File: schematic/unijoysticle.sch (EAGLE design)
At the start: 8 parts, among them CN1 DC JACK, IC1 4066N, IC2 4066N, IC3 4066N, J1 DB9, J2 DB9

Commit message: fix: yet another pcb version. smaller, better design
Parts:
- MOD1: value NodeMCU Amica v1.0 -> ESP12E_DEVKIT; OC_NEWARK unknown -> (none)
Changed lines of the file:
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@@
 </classes>
 <parts>
-<part name="MOD1" library="ESP12E_DEVKIT" deviceset="ESP12E_DEVKIT" device="" value="NodeMCU Amica v1.0">
-<attribute name="MF" value=""/>
-<attribute name="MPN" value=""/>
-<attribute name="OC_NEWARK" value="unknown"/>
-</part>
 <part name="IC1" library="40xx" deviceset="4066" device="N">
 <attribute name="MF" value="TEXAS INSTRUMENTS"/>
@@
 <attribute name="OC_NEWARK" value="16T0655"/>
 </part>
+<part name="MOD1" library="ESP12E_DEVKIT" deviceset="ESP12E_DEVKIT" device=""/>
 </parts>
 <sheets>
@@
 </plain>
 <instances>
-<instance part="MOD1" gate="G$1" x="116.84" y="25.4" rot="R90">
-<attribute name="OC_NEWARK" x="116.84" y="25.4" size="1.778" layer="96" display="off"/>
-<attribute name="MF" x="116.84" y="25.4" size="1.778" layer="96" display="off"/>
-<attribute name="MPN" x="116.84" y="25.4" size="1.778" layer="96" display="off"/>
-</instance>
 <instance part="IC1" gate="A" x="68.58" y="139.7">
 <attribute name="OC_NEWARK" x="68.58" y="139.7" size="1.778" layer="96" display="off"/>
@@
 <attribute name="MPN" x="154.94" y="170.18" size="1.778" layer="96" display="off"/>
 </instance>
+<instance part="MOD1" gate="G$1" x="116.84" y="25.4" rot="R90"/>
 </instances>
 <busses>
@@
 <net name="N$1" class="0">
 <segment>
-<pinref part="MOD1" gate="G$1" pin="D0"/>
 <wire x1="99.06" y1="43.18" x2="99.06" y2="48.26" width="0.1524" layer="91"/>
 <wire x1="99.06" y1="48.26" x2="22.86" y2="48.26" width="0.1524" layer="91"/>
@@
 <pinref part="IC1" gate="A" pin="C"/>
 <wire x1="22.86" y1="137.16" x2="55.88" y2="137.16" width="0.1524" layer="91"/>
+<pinref part="MOD1" gate="G$1" pin="D0"/>
 </segment>
 </net>
 <net name="N$2" class="0">
 <segment>
-<pinref part="MOD1" gate="G$1" pin="D1"/>
 <wire x1="101.6" y1="43.18" x2="101.6" y2="50.8" width="0.1524" layer="91"/>
 <wire x1="101.6" y1="50.8" x2="25.4" y2="50.8" width="0.1524" layer="91"/>
@@
 <pinref part="IC1" gate="B" pin="C"/>
 <wire x1="25.4" y1="119.38" x2="55.88" y2="119.38" width="0.1524" layer="91"/>
+<pinref part="MOD1" gate="G$1" pin="D1"/>
 </segment>
 </net>
 <net name="N$3" class="0">
 <segment>
-<pinref part="MOD1" gate="G$1" pin="D2"/>
 <wire x1="104.14" y1="43.18" x2="104.14" y2="53.34" width="0.1524" layer="91"/>
 <wire x1="104.14" y1="53.34" x2="27.94" y2="53.34" width="0.1524" layer="91"/>
@@
 <pinref part="IC1" gate="C" pin="C"/>
 <wire x1="27.94" y1="101.6" x2="55.88" y2="101.6" width="0.1524" layer="91"/>
+<pinref part="MOD1" gate="G$1" pin="D2"/>
 </segment>
 </net>
 <net name="N$4" class="0">
 <segment>
-<pinref part="MOD1" gate="G$1" pin="D3"/>
 <wire x1="106.68" y1="43.18" x2="106.68" y2="55.88" width="0.1524" layer="91"/>
 <wire x1="106.68" y1="55.88" x2="30.48" y2="55.88" width="0.1524" layer="91"/>
@@
 <pinref part="IC1" gate="D" pin="C"/>
 <wire x1="30.48" y1="83.82" x2="55.88" y2="83.82" width="0.1524" layer="91"/>
+<pinref part="MOD1" gate="G$1" pin="D3"/>
 </segment>
 </net>
 <net name="N$5" class="0">
 <segment>
-<pinref part="MOD1" gate="G$1" pin="D5"/>
 <wire x1="116.84" y1="43.18" x2="116.84" y2="137.16" width="0.1524" layer="91"/>
 <pinref part="IC3" gate="A" pin="C"/>
 <wire x1="116.84" y1="137.16" x2="142.24" y2="137.16" width="0.1524" layer="91"/>
+<pinref part="MOD1" gate="G$1" pin="D5"/>
 </segment>
 </net>
 <net name="N$6" class="0">
 <segment>
-<pinref part="MOD1" gate="G$1" pin="D6"/>
 <wire x1="119.38" y1="43.18" x2="119.38" y2="119.38" width="0.1524" layer="91"/>
 <pinref part="IC3" gate="B" pin="C"/>
 <wire x1="119.38" y1="119.38" x2="142.24" y2="119.38" width="0.1524" layer="91"/>
+<pinref part="MOD1" gate="G$1" pin="D6"/>
 </segment>
 </net>
 <net name="N$7" class="0">
 <segment>
-<pinref part="MOD1" gate="G$1" pin="D7"/>
 <wire x1="121.92" y1="43.18" x2="121.92" y2="101.6" width="0.1524" layer="91"/>
 <pinref part="IC3" gate="C" pin="C"/>
 <wire x1="121.92" y1="101.6" x2="142.24" y2="101.6" width="0.1524" layer="91"/>
+<pinref part="MOD1" gate="G$1" pin="D7"/>
 </segment>
 </net>
 <net name="N$8" class="0">
 <segment>
-<pinref part="MOD1" gate="G$1" pin="D8"/>
 <wire x1="124.46" y1="43.18" x2="124.46" y2="83.82" width="0.1524" layer="91"/>
 <pinref part="IC3" gate="D" pin="C"/>
 <wire x1="124.46" y1="83.82" x2="142.24" y2="83.82" width="0.1524" layer="91"/>
+<pinref part="MOD1" gate="G$1" pin="D8"/>
 </segment>
 </net>
@@
 </segment>
 <segment>
-<pinref part="MOD1" gate="G$1" pin="GND@3"/>
 <wire x1="132.08" y1="43.18" x2="132.08" y2="55.88" width="0.1524" layer="91"/>
 <wire x1="132.08" y1="55.88" x2="137.16" y2="55.88" width="0.1524" layer="91"/>
 <pinref part="GND3" gate="1" pin="GND"/>
 <wire x1="137.16" y1="55.88" x2="137.16" y2="53.34" width="0.1524" layer="91"/>
+<pinref part="MOD1" gate="G$1" pin="GND@3"/>
 </segment>
 </net>
@@
 </segment>
 <segment>
-<pinref part="MOD1" gate="G$1" pin="3V3@2"/>
 <pinref part="P+1" gate="VCC" pin="VCC"/>
 <wire x1="134.62" y1="43.18" x2="144.78" y2="43.18" width="0.1524" layer="91"/>
 <wire x1="144.78" y1="43.18" x2="144.78" y2="50.8" width="0.1524" layer="91"/>
+<pinref part="MOD1" gate="G$1" pin="3V3@2"/>
 </segment>
 </net>
 <net name="N$19" class="0">
 <segment>
-<pinref part="MOD1" gate="G$1" pin="D4"/>
 <wire x1="109.22" y1="43.18" x2="109.22" y2="58.42" width="0.1524" layer="91"/>
 <wire x1="109.22" y1="58.42" x2="50.8" y2="58.42" width="0.1524" layer="91"/>
@@
 <pinref part="IC2" gate="A" pin="C"/>
 <wire x1="50.8" y1="66.04" x2="55.88" y2="66.04" width="0.1524" layer="91"/>
+<pinref part="MOD1" gate="G$1" pin="D4"/>
 </segment>
 </net>
 <net name="N$20" class="0">
 <segment>
-<pinref part="MOD1" gate="G$1" pin="RX"/>
 <wire x1="127" y1="43.18" x2="127" y2="66.04" width="0.1524" layer="91"/>
 <pinref part="IC2" gate="B" pin="C"/>
 <wire x1="127" y1="66.04" x2="142.24" y2="66.04" width="0.1524" layer="91"/>
+<pinref part="MOD1" gate="G$1" pin="RX"/>
 </segment>
 </net>
@@
 <segment>
 <pinref part="SUPPLY2" gate="G$1" pin="5V"/>
+<wire x1="139.7" y1="7.62" x2="134.62" y2="7.62" width="0.1524" layer="91"/>
 <pinref part="MOD1" gate="G$1" pin="VIN"/>
-<wire x1="139.7" y1="7.62" x2="134.62" y2="7.62" width="0.1524" layer="91"/>
 </segment>
 </net>
@@
 </segment>
 <segment>
-<pinref part="MOD1" gate="G$1" pin="GND@1"/>
 <pinref part="GND2" gate="G$1" pin="3.3V"/>
 <wire x1="132.08" y1="0" x2="132.08" y2="7.62" width="0.1524" layer="91"/>
-</segment>
-</net>
+<pinref part="MOD1" gate="G$1" pin="GND@1"/>
+</segment>
+</net>

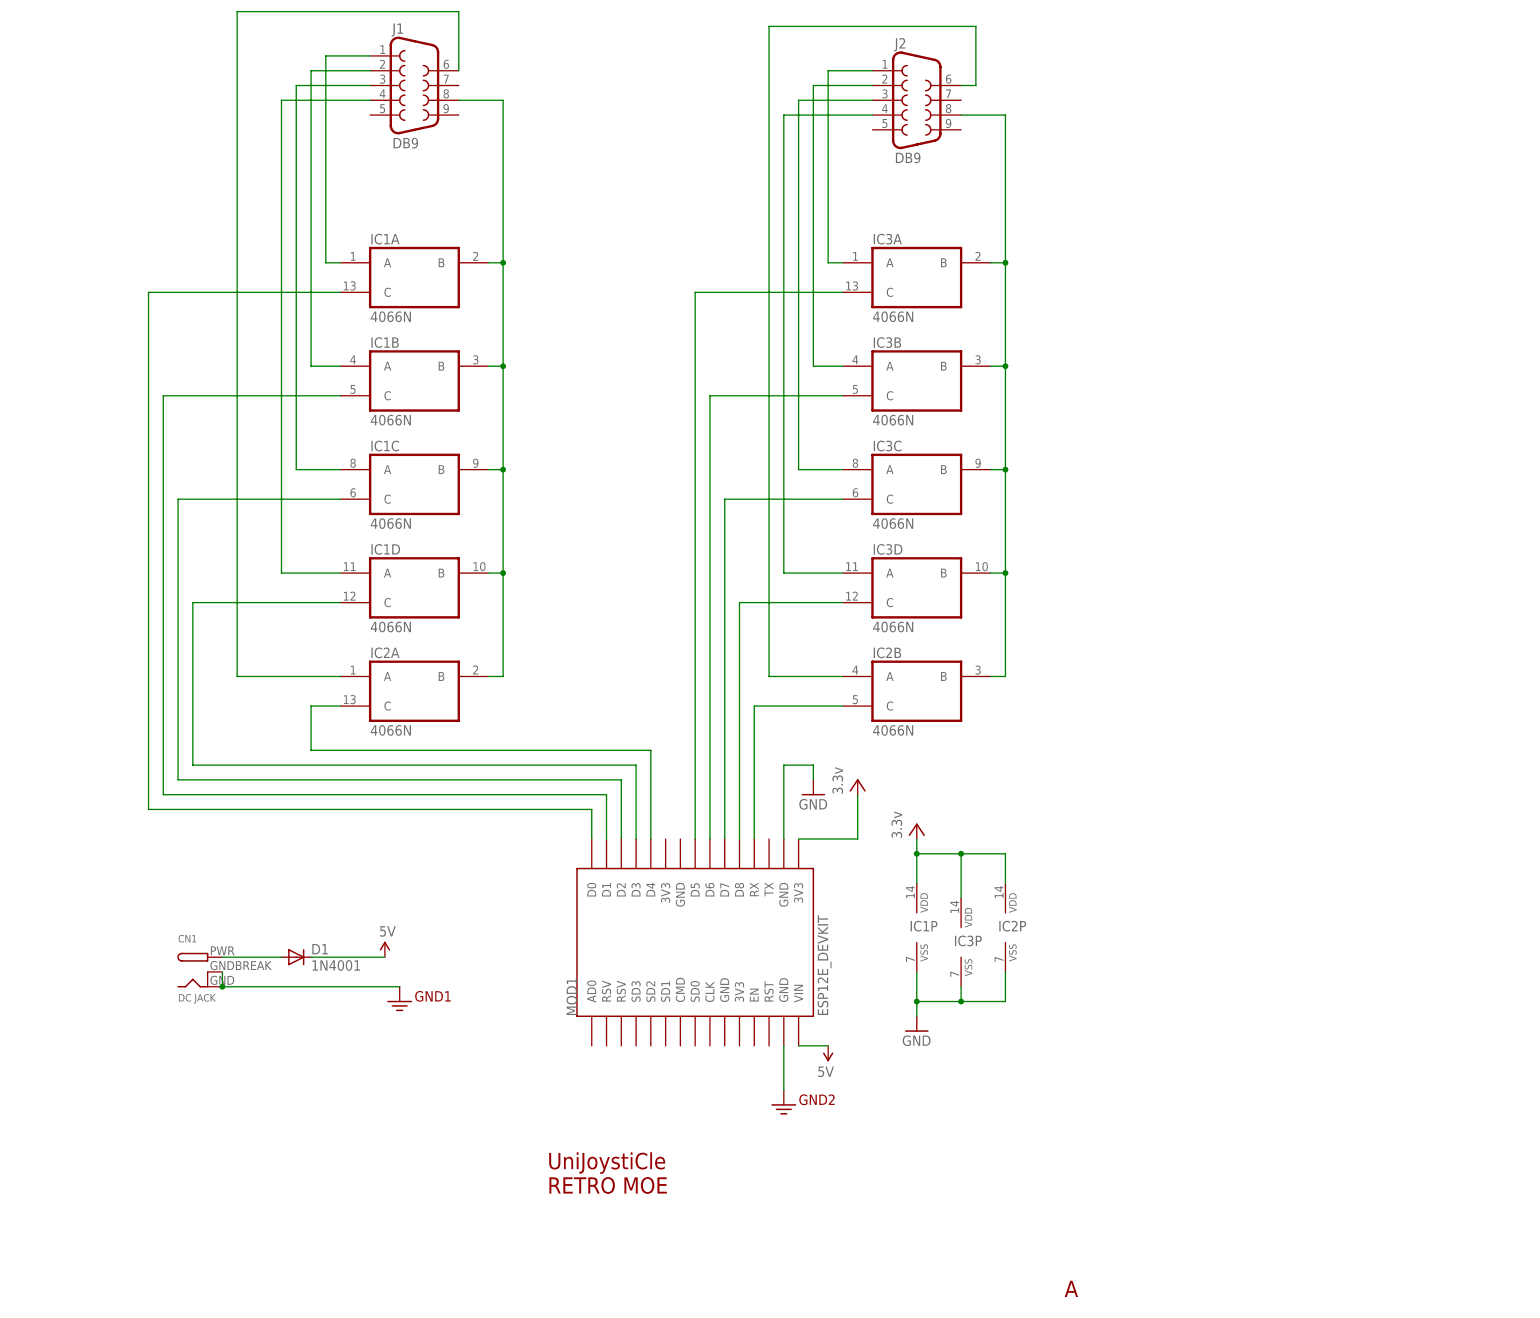
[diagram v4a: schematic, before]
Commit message: fix: adds .cam file to generate gerbert files
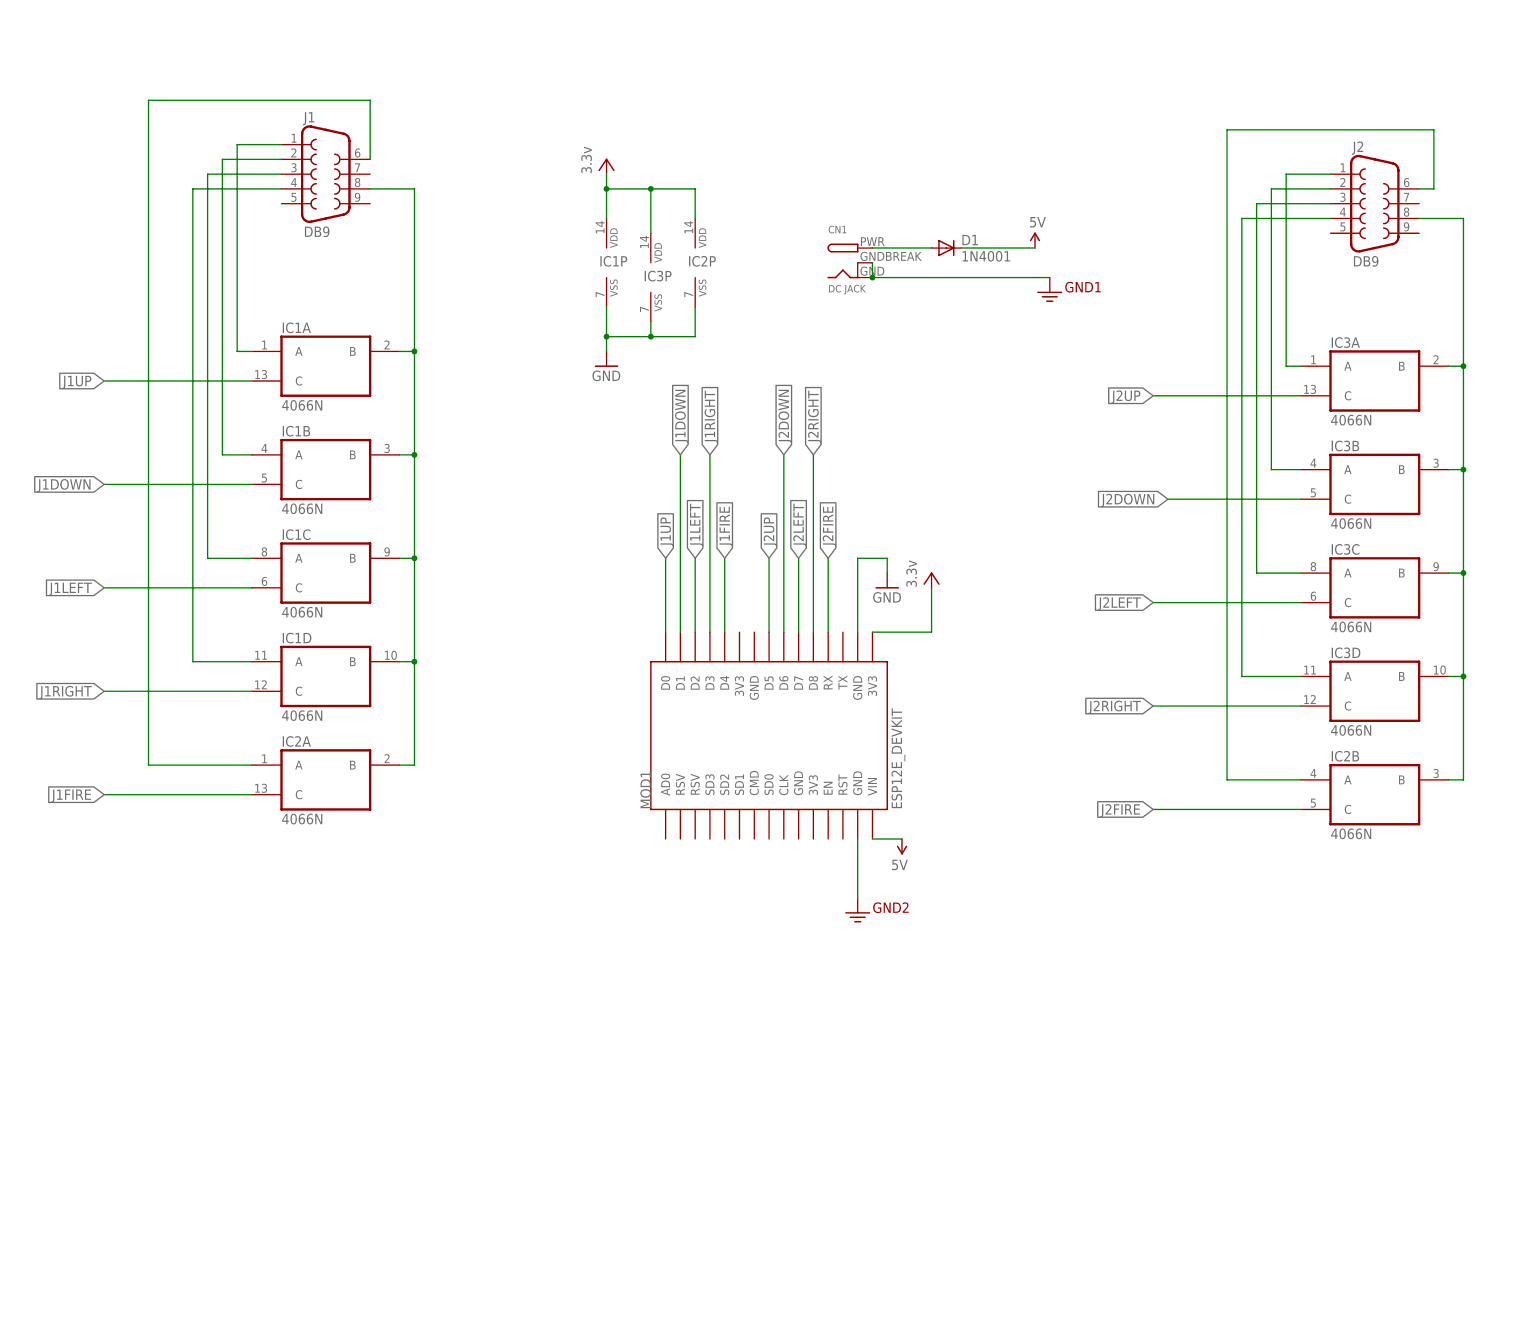
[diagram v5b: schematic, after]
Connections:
- net N$1 renamed J1UP
- net N$19 renamed J1FIRE
- net N$2 renamed J1DOWN
- net N$20 renamed J2FIRE
- net N$3 renamed J1LEFT
- net N$4 renamed J1RIGHT
- net N$5 renamed J2UP
- net N$6 renamed J2DOWN
- net N$7 renamed J2LEFT
- net N$8 renamed J2RIGHT
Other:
- note removed: "A"
- note removed: "UniJoystiCle RETRO MOE"
- moved on the sheet: CN1, D1, IC1A, IC1B, IC1C, IC1D, IC1P, IC2A, IC2B, IC2P, IC3A, IC3B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

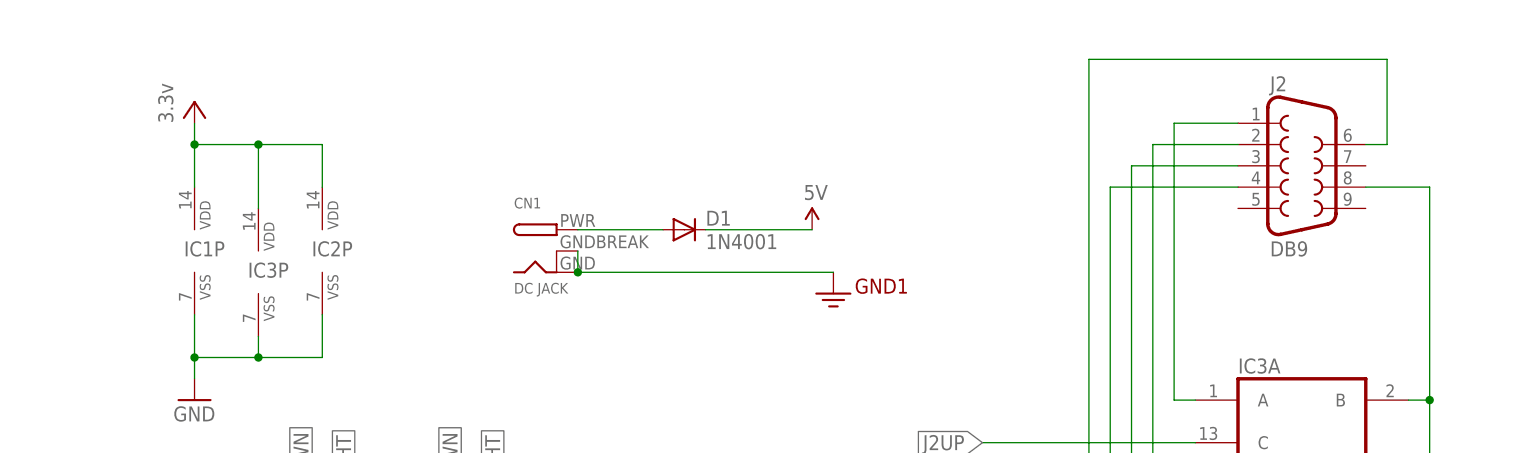
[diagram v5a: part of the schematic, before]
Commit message: fix: esp8622 schematic: ics with joy power. new dc jack barrel
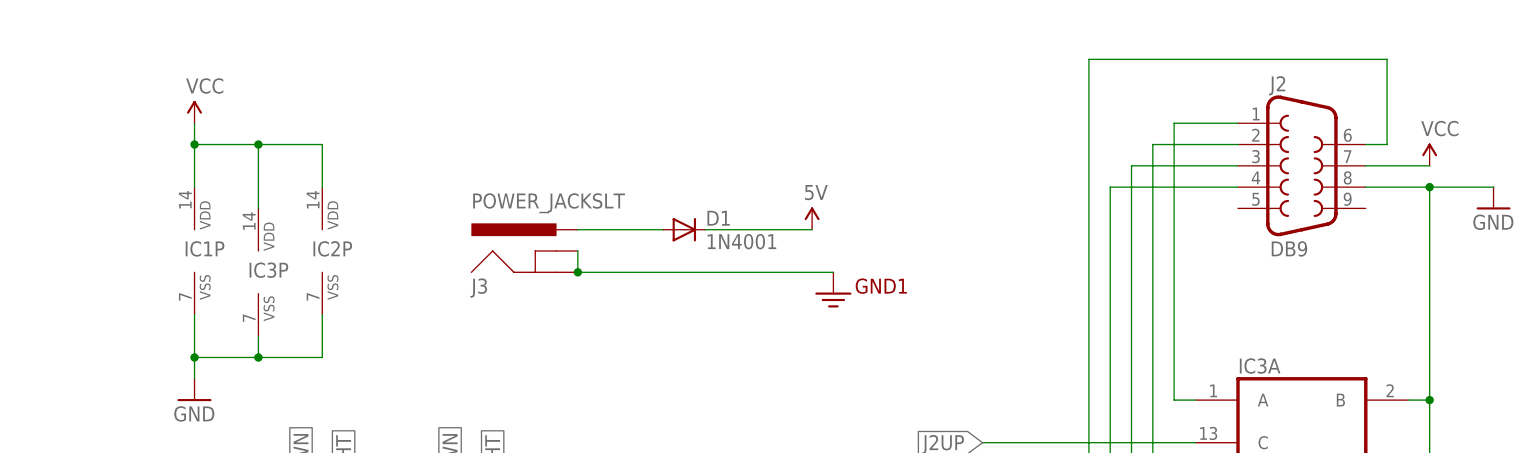
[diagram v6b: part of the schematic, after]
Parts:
- removed CN1: DC JACK, adafruit:DCBARRELPTH
- added J3: POWER_JACKSLT, SparkFun-Connectors:POWER_JACKSLT
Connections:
- removed net N$18: IC2B.B, IC3A.B, IC3B.B, IC3C.B, IC3D.B, J2.8
- net 3.3V: now also J3.GND, J3.GNDBREAK; no longer CN1.GND, CN1.GNDBREAK
- net GND: now also IC2B.B, IC3A.B, IC3B.B, IC3C.B, IC3D.B, J2.8
- net N$23: now also J3.PWR; no longer CN1.PWR
- net VCC: now also J2.7

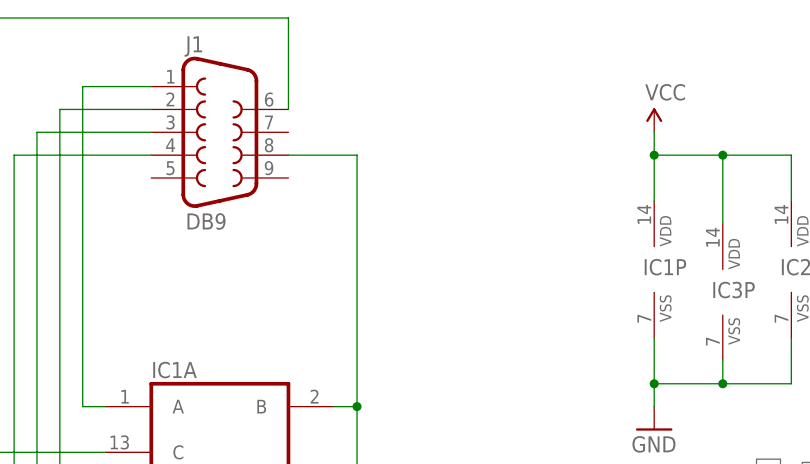
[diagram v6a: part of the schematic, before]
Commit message: fix: joy pin #8 are connected
Not really needed since they are already connected inside the C64,
but usuful to have them connected in the board
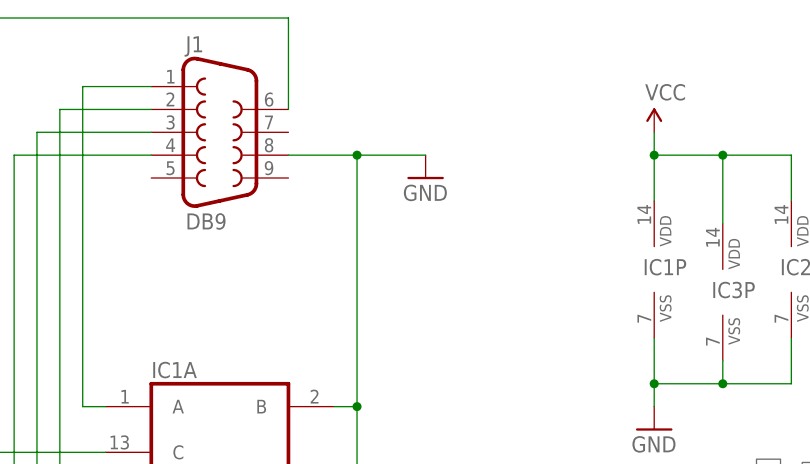
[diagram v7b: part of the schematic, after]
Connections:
- removed net N$2: IC1A.B, IC1B.B, IC1C.B, IC1D.B, IC2A.B, J1.8
- net GND: now also IC1A.B, IC1B.B, IC1C.B, IC1D.B, IC2A.B, J1.8
